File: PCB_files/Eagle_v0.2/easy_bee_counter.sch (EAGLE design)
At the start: 129 parts, among them J1 S_5V, J3 S_LOAD, J4 S_I2C, Q6 60V/32A/35mΩ, Q7 60V/32A/35mΩ, U01I QRE1113_QRE1113_, U01O QRE1113_QRE1113_, U02I QRE1113_QRE1113_, U02O QRE1113_QRE1113_, U03I QRE1113_QRE1113_, U03O QRE1113_QRE1113_, U04I QRE1113_QRE1113_, U04O QRE1113_QRE1113_, U05I QRE1113_QRE1113_, U05O QRE1113_QRE1113_, U06I QRE1113_QRE1113_, U06O QRE1113_QRE1113_, U07I QRE1113_QRE1113_, U07O QRE1113_QRE1113_, U08I QRE1113_QRE1113_, U08O QRE1113_QRE1113_, U09I QRE1113_QRE1113_, U09O QRE1113_QRE1113_, U1 74*165, U10I QRE1113_QRE1113_, U10O QRE1113_QRE1113_, U11I QRE1113_QRE1113_, U11O QRE1113_QRE1113_, U12I QRE1113_QRE1113_, U12O QRE1113_QRE1113_, U13I QRE1113_QRE1113_, U13O QRE1113_QRE1113_, U14I QRE1113_QRE1113_, U14O QRE1113_QRE1113_, U15I QRE1113_QRE1113_, U15O QRE1113_QRE1113_, U16I QRE1113_QRE1113_, U16O QRE1113_QRE1113_, U17I QRE1113_QRE1113_, U17O QRE1113_QRE1113_, U18I QRE1113_QRE1113_, U18O QRE1113_QRE1113_, U19I QRE1113_QRE1113_, U19O QRE1113_QRE1113_, U2 74*165, U20I QRE1113_QRE1113_, U20O QRE1113_QRE1113_, U21I QRE1113_QRE1113_, U21O QRE1113_QRE1113_, U22I QRE1113_QRE1113_, U22O QRE1113_QRE1113_, U23I QRE1113_QRE1113_, U23O QRE1113_QRE1113_, U24I QRE1113_QRE1113_, U24O QRE1113_QRE1113_, U3 74*165, U4 74*165, U5 74*165, U6 74*165, U7 R78E3.3-1.0

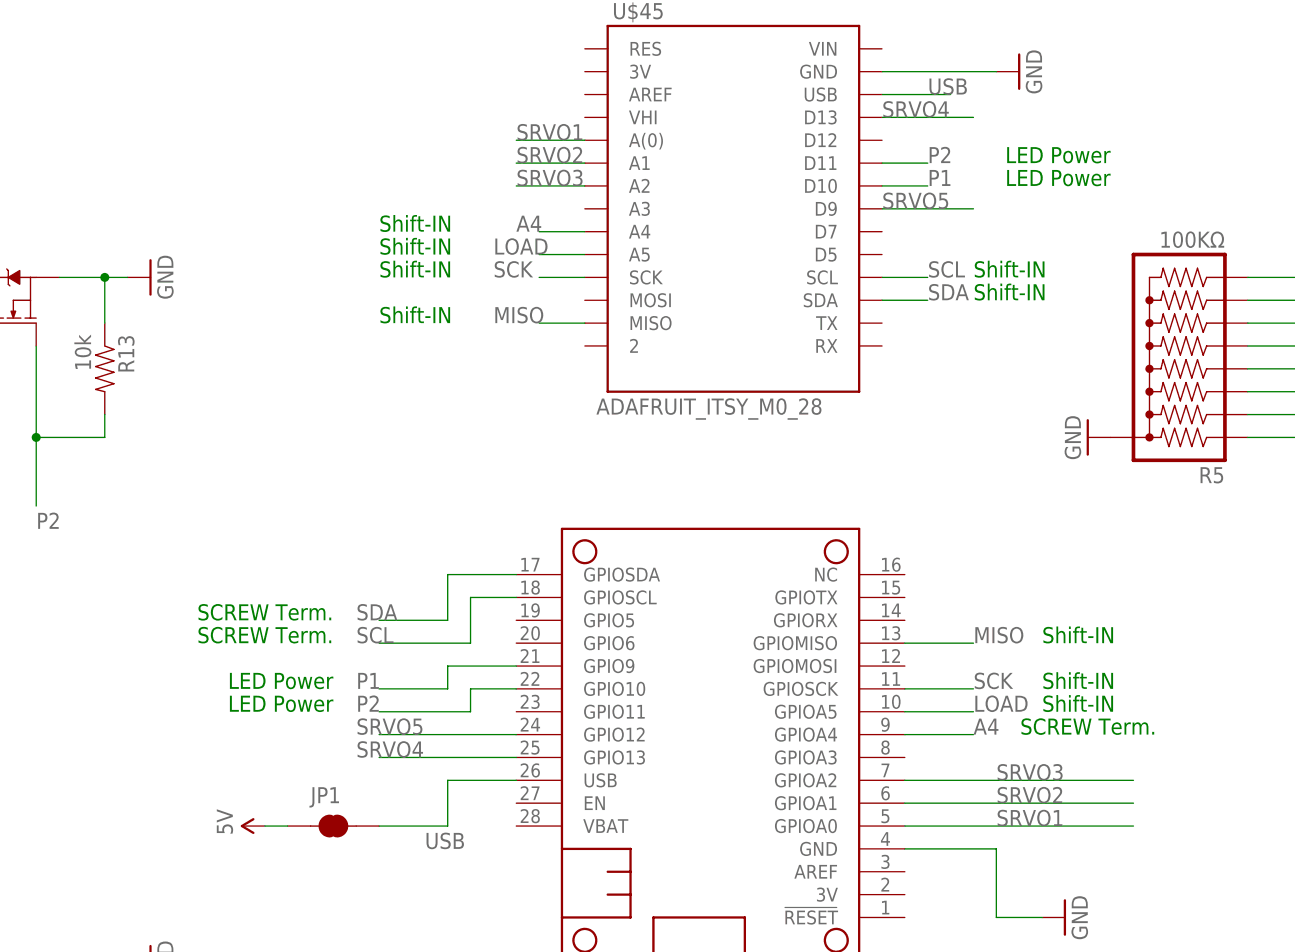
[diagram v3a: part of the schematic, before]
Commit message: Corrected unusable pins for servos
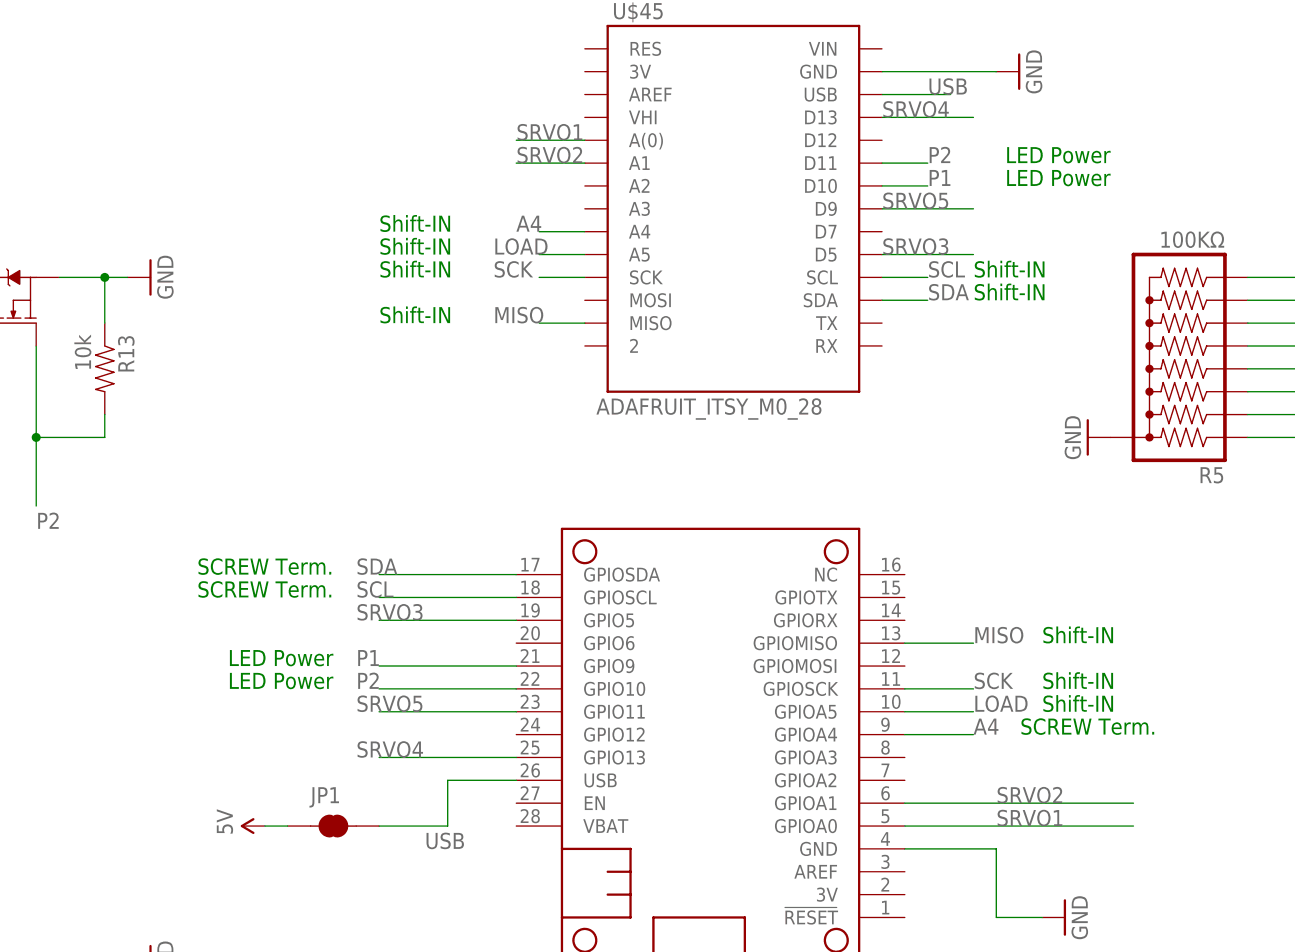
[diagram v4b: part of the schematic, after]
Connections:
- net SRVO3: now also MS2.GPIO5, U$45.D5; no longer MS2.GPIOA2, U$45.A2
- net SRVO5: now also MS2.GPIO11; no longer MS2.GPIO12
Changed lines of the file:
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@@
 <text x="-195.58" y="993.14" size="1.778" layer="91">Shift-IN</text>
 <text x="-195.58" y="995.68" size="1.778" layer="91">Shift-IN</text>
+<text x="-274.32" y="998.22" size="1.778" layer="91" align="bottom-right">LED Power</text>
 <text x="-274.32" y="995.68" size="1.778" layer="91" align="bottom-right">LED Power</text>
-<text x="-274.32" y="993.14" size="1.778" layer="91" align="bottom-right">LED Power</text>
-<text x="-274.32" y="1003.3" size="1.778" layer="91" align="bottom-right">SCREW Term.</text>
-<text x="-274.32" y="1000.76" size="1.778" layer="91" align="bottom-right">SCREW Term.</text>
+<text x="-274.32" y="1008.38" size="1.778" layer="91" align="bottom-right">SCREW Term.</text>
+<text x="-274.32" y="1005.84" size="1.778" layer="91" align="bottom-right">SCREW Term.</text>
 <text x="-182.88" y="990.6" size="1.778" layer="91" align="bottom-right">SCREW Term.</text>
 <text x="-246.38" y="922.02" size="1.778" layer="91" align="bottom-right">SCREW Term.</text>
@@
 <net name="SCL" class="0">
 <segment>
-<label x="-271.78" y="1000.76" size="1.778" layer="95"/>
-<wire x1="-269.24" y1="1000.76" x2="-259.08" y2="1000.76" width="0.1524" layer="91"/>
-<wire x1="-259.08" y1="1000.76" x2="-259.08" y2="1005.84" width="0.1524" layer="91"/>
+<label x="-271.78" y="1005.84" size="1.778" layer="95"/>
+<wire x1="-269.24" y1="1005.84" x2="-254" y2="1005.84" width="0.1524" layer="91"/>
 <pinref part="MS2" gate="G$1" pin="GPIOSCL"/>
-<wire x1="-259.08" y1="1005.84" x2="-254" y2="1005.84" width="0.1524" layer="91"/>
 </segment>
 <segment>
@@
 <net name="P1" class="0">
 <segment>
-<label x="-271.78" y="995.68" size="1.778" layer="95"/>
-<wire x1="-269.24" y1="995.68" x2="-261.62" y2="995.68" width="0.1524" layer="91"/>
-<wire x1="-261.62" y1="995.68" x2="-261.62" y2="998.22" width="0.1524" layer="91"/>
+<label x="-271.78" y="998.22" size="1.778" layer="95"/>
 <pinref part="MS2" gate="G$1" pin="GPIO9"/>
-<wire x1="-261.62" y1="998.22" x2="-254" y2="998.22" width="0.1524" layer="91"/>
+<wire x1="-269.24" y1="998.22" x2="-254" y2="998.22" width="0.1524" layer="91"/>
 </segment>
 <segment>
@@
 <net name="SDA" class="0">
 <segment>
-<wire x1="-261.62" y1="1003.3" x2="-269.24" y2="1003.3" width="0.1524" layer="91"/>
-<label x="-271.78" y="1003.3" size="1.778" layer="95"/>
+<label x="-271.78" y="1008.38" size="1.778" layer="95"/>
 <pinref part="MS2" gate="G$1" pin="GPIOSDA"/>
-<wire x1="-261.62" y1="1003.3" x2="-261.62" y2="1008.38" width="0.1524" layer="91"/>
-<wire x1="-261.62" y1="1008.38" x2="-254" y2="1008.38" width="0.1524" layer="91"/>
+<wire x1="-269.24" y1="1008.38" x2="-254" y2="1008.38" width="0.1524" layer="91"/>
 </segment>
 <segment>
@@
 <net name="P2" class="0">
 <segment>
-<label x="-271.78" y="993.14" size="1.778" layer="95"/>
+<label x="-271.78" y="995.68" size="1.778" layer="95"/>
 <pinref part="MS2" gate="G$1" pin="GPIO10"/>
-<wire x1="-254" y1="995.68" x2="-259.08" y2="995.68" width="0.1524" layer="91"/>
-<wire x1="-259.08" y1="995.68" x2="-259.08" y2="993.14" width="0.1524" layer="91"/>
-<wire x1="-259.08" y1="993.14" x2="-269.24" y2="993.14" width="0.1524" layer="91"/>
+<wire x1="-254" y1="995.68" x2="-269.24" y2="995.68" width="0.1524" layer="91"/>
 </segment>
 <segment>
@@
 </segment>
 <segment>
-<pinref part="MS2" gate="G$1" pin="GPIOA2"/>
-<wire x1="-210.82" y1="985.52" x2="-185.42" y2="985.52" width="0.1524" layer="91"/>
-<label x="-200.66" y="985.52" size="1.778" layer="95"/>
+<label x="-271.78" y="1003.3" size="1.778" layer="95"/>
+<pinref part="MS2" gate="G$1" pin="GPIO5"/>
+<wire x1="-254" y1="1003.3" x2="-269.24" y2="1003.3" width="0.1524" layer="91"/>
 </segment>
 <segment>
-<pinref part="U$45" gate="G$1" pin="A2"/>
-<wire x1="-246.38" y1="1051.56" x2="-254" y2="1051.56" width="0.1524" layer="91"/>
-<label x="-254" y="1051.56" size="1.778" layer="95"/>
+<label x="-213.36" y="1043.94" size="1.778" layer="95"/>
+<pinref part="U$45" gate="G$1" pin="D5"/>
+<wire x1="-213.36" y1="1043.94" x2="-203.2" y2="1043.94" width="0.1524" layer="91"/>
 </segment>
 </net>
@@
 </segment>
 <segment>
-<pinref part="MS2" gate="G$1" pin="GPIO12"/>
-<wire x1="-254" y1="990.6" x2="-269.24" y2="990.6" width="0.1524" layer="91"/>
-<label x="-271.78" y="990.6" size="1.778" layer="95"/>
+<label x="-271.78" y="993.14" size="1.778" layer="95"/>
+<pinref part="MS2" gate="G$1" pin="GPIO11"/>
+<wire x1="-254" y1="993.14" x2="-269.24" y2="993.14" width="0.1524" layer="91"/>
 </segment>
 <segment>
